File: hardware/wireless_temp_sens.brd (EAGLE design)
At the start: 100 x 80 mm, 32 parts, among them Q1 BC550C, Q2 32.768kHz, Q3 1MHz

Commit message: update board schema
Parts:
- removed C6, C7: 30pF, rcl:C025-024X044
- removed Q3: 1MHz, crystal:HC49/S
- moved C4 96.5 mm to (10.8, 22.4), turned to 90 degrees
- moved SUPPLY 86.7 mm to (15.7, 72.1), turned to 270 degrees
- moved UC1 65.5 mm to (75.2, 20.5), turned to 180 degrees
- moved R10 54.9 mm to (78.3, 38.8), turned to 270 degrees
- moved R9 52.3 mm to (78.3, 51.9), turned to 270 degrees
- moved C8 52.1 mm to (22.4, 23.9), turned to 180 degrees
- moved UC2 51.5 mm to (34.1, 13.5), turned to 0 degrees
- moved C1 51.0 mm to (57.2, 6.37), turned to 90 degrees
- moved C9 49.5 mm to (22.4, 15.8), turned to 180 degrees
- moved U$6 48.7 mm to (72.4, 49.6)
- moved R8 48.6 mm to (63.8, 48.6)
- moved C5 42.5 mm to (59.2, 48.4)
- moved R2 42.2 mm to (36.5, 5.43)
- moved R3 42.1 mm to (36.2, 9.13)
- moved UC3 41.5 mm to (44.1, 69.0), turned to 0 degrees
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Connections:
- net GND: no longer C6.2, C7.2
- net OSC1: no longer C6.1, Q3.2
- net OSC2: no longer C7.1, Q3.1
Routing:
- net BATTSENS: track 19.2 -> 60.3 mm, vias 2 -> 4
- net GND: track 335.9 -> 303.7 mm, vias 6 -> 0
- net UART_RX: track 81.5 -> 57.6 mm, vias 0 -> 2
- net VCC: track 185.6 -> 207.1 mm, vias 6 -> 4
- net N$4: track 54.4 -> 33.1 mm
- net N$7: track 4.32 -> 19.9 mm
- net LED_GREEN: track 4.06 -> 18.1 mm
- net SDA: track 34.2 -> 47.1 mm, vias 2 -> 4
- net SCL: track 53.2 -> 40.7 mm, vias 0 -> 2
- net N$1: track 33.0 -> 21.8 mm, vias 0 -> 2
- net UART_TX: track 83.0 -> 72.0 mm, vias 0 -> 2
- net PGC: track 3.81 -> 13.2 mm, vias 0 -> 2
- net N$6: track 6.10 -> 15.1 mm
- net PGD: track 4.17 -> 13.1 mm, vias 0 -> 2
- net PGM: track 3.81 -> 12.5 mm, vias 0 -> 2
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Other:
- board size 100 x 80 mm -> 90 x 83 mm

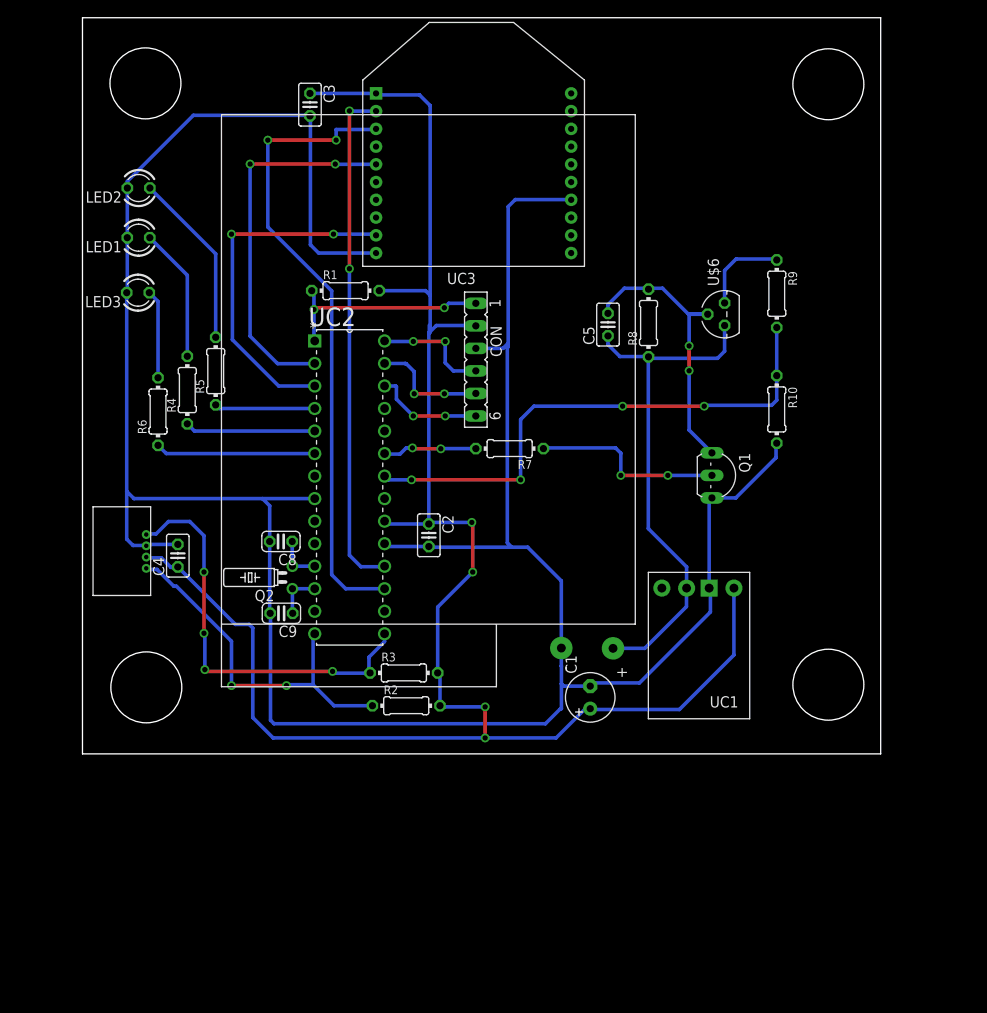
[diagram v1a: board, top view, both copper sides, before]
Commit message: update schematic with G300 box
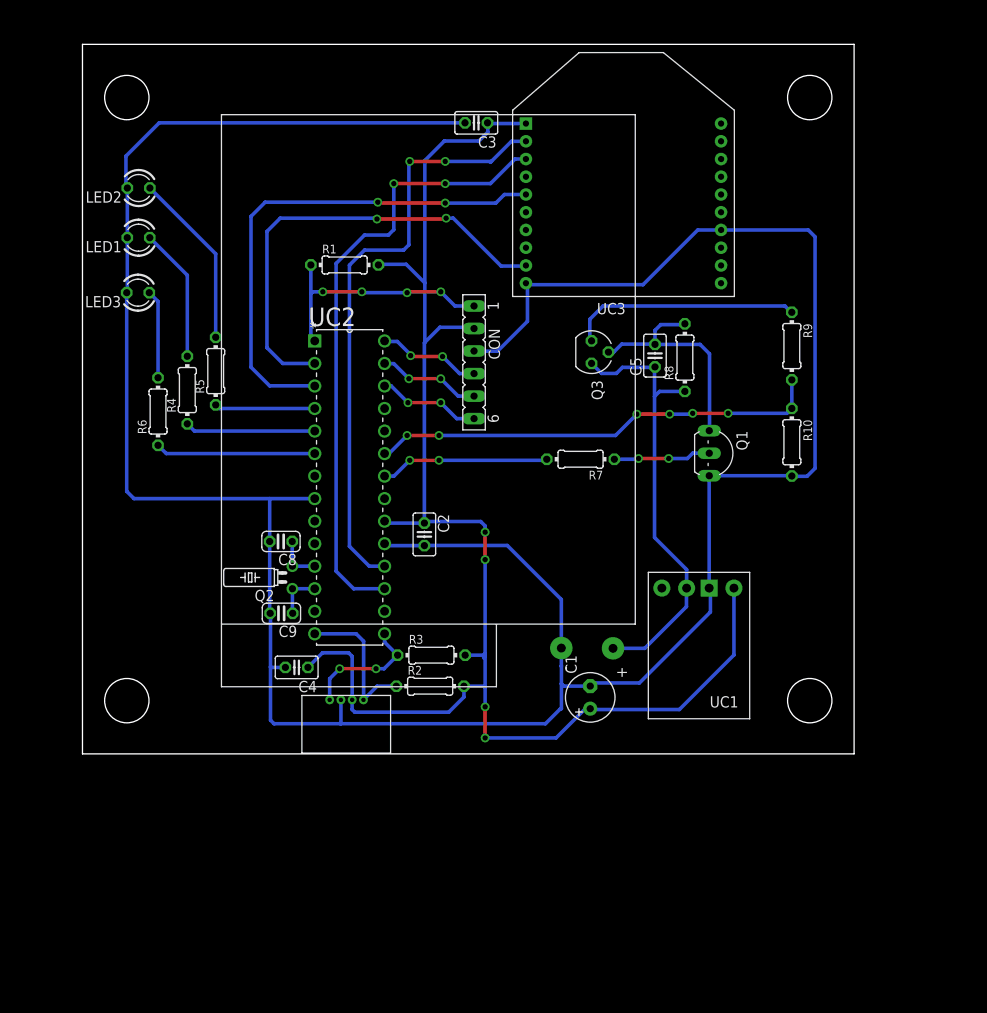
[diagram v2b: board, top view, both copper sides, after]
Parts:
- removed U$6: BS250P, ma_libs:TO92
- added Q3: BS250, transistor-small-signal:SOT54E
- moved UC4 27.3 mm to (24.7, 6.59), turned to 0 degrees
- moved C3 18.9 mm to (44.4, 71.2), turned to 180 degrees
- moved C4 18.4 mm to (24.1, 9.75), turned to 180 degrees
- moved UC3 17.2 mm to (61.0, 65.6)
- moved R7 8.09 mm to (56.2, 33.2)
- moved C5 6.35 mm to (64.5, 44.9)
- moved R9 6.14 mm to (80.0, 46.0)
- moved R8 5.66 mm to (67.9, 44.7)
- moved R10 4.07 mm to (80.0, 35.1)
- moved R3 3.69 mm to (39.3, 11.1)
- moved R2 3.48 mm to (39.2, 7.63)
- moved R1 2.90 mm to (29.6, 55.1)
- moved Q1 2.52 mm to (71.9, 33.9)
- moved C2 0.51 mm to (38.5, 24.8)
- moved CON 0.36 mm to (44.1, 44.1)
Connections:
- removed net N$5: R9.1, U$6.1
- new net N$3: Q3.D, R9.1
- net BATTSENS: now also UC2.23; no longer UC2.22
- net BATTSEN_EN: now also UC2.22; no longer UC2.23
- net N$4: now also Q3.G; no longer U$6.2
- net V_BATT: now also Q3.S; no longer U$6.3
- net XBEE_RESET: now also UC2.3; no longer UC2.2
- net XBEE_SLEEP_RQ: now also UC2.2; no longer UC2.3
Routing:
- net VCC: track 207.1 -> 174.0 mm
- net SDA: track 47.1 -> 14.2 mm, vias 4 -> 2
- net N$3: track 0.00 -> 26.2 mm
- net SCL: track 40.7 -> 16.8 mm, vias 2 -> 0
- net XBEE_RESET: track 42.2 -> 57.2 mm
- net GND: track 303.7 -> 318.5 mm
- net XBEE_SLEEP_RQ: track 39.7 -> 51.4 mm
- net N$1: track 21.8 -> 11.0 mm
- net UART_RX: track 57.6 -> 68.0 mm
- net N$5: track 10.1 -> 0.00 mm
- net BATTSENS: track 60.3 -> 51.2 mm, vias 4 -> 6
- net BATTSEN_EN: track 10.7 -> 19.1 mm
- net V_BATT: track 58.2 -> 50.3 mm
- net N$4: track 33.1 -> 26.2 mm, vias 2 -> 0
- net N$2: track 24.3 -> 28.0 mm, vias 2 -> 4
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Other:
- board size 90 x 83 mm -> 87 x 80 mm

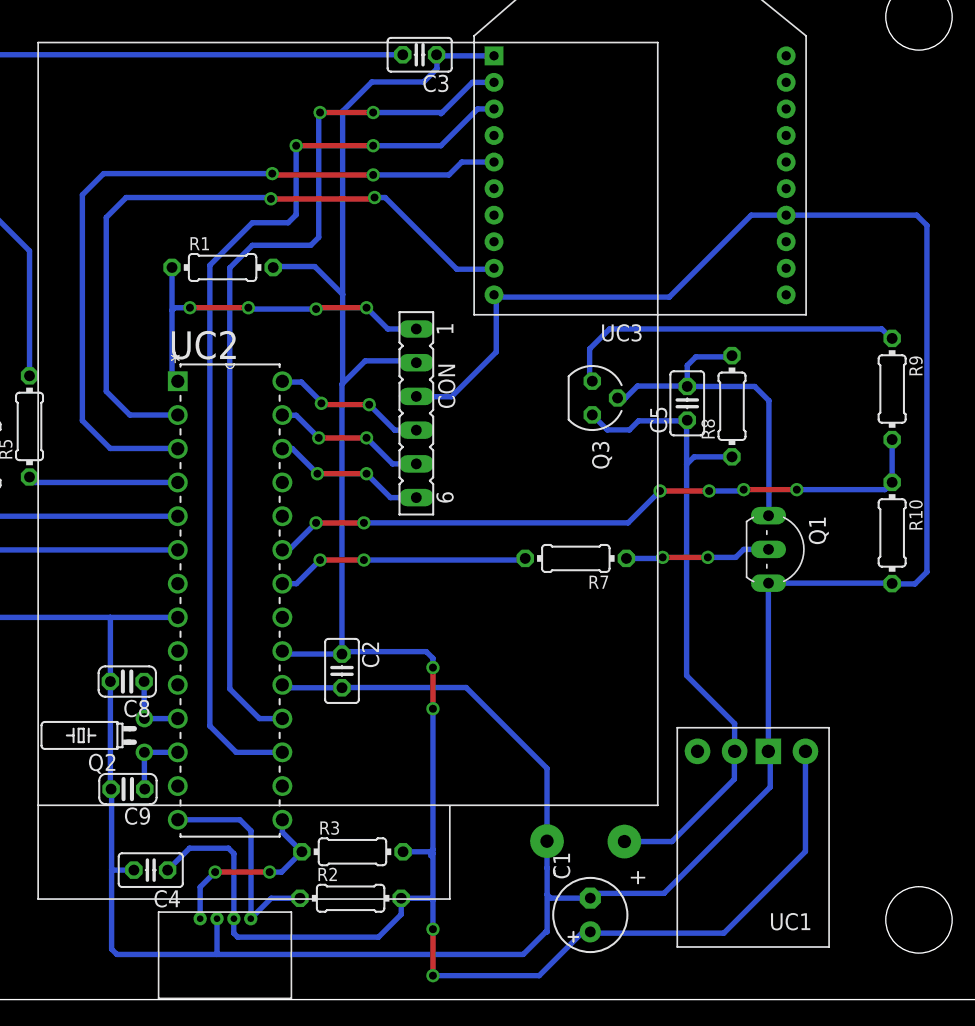
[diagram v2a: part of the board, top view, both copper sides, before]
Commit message: add 2.54mm connector for I2C
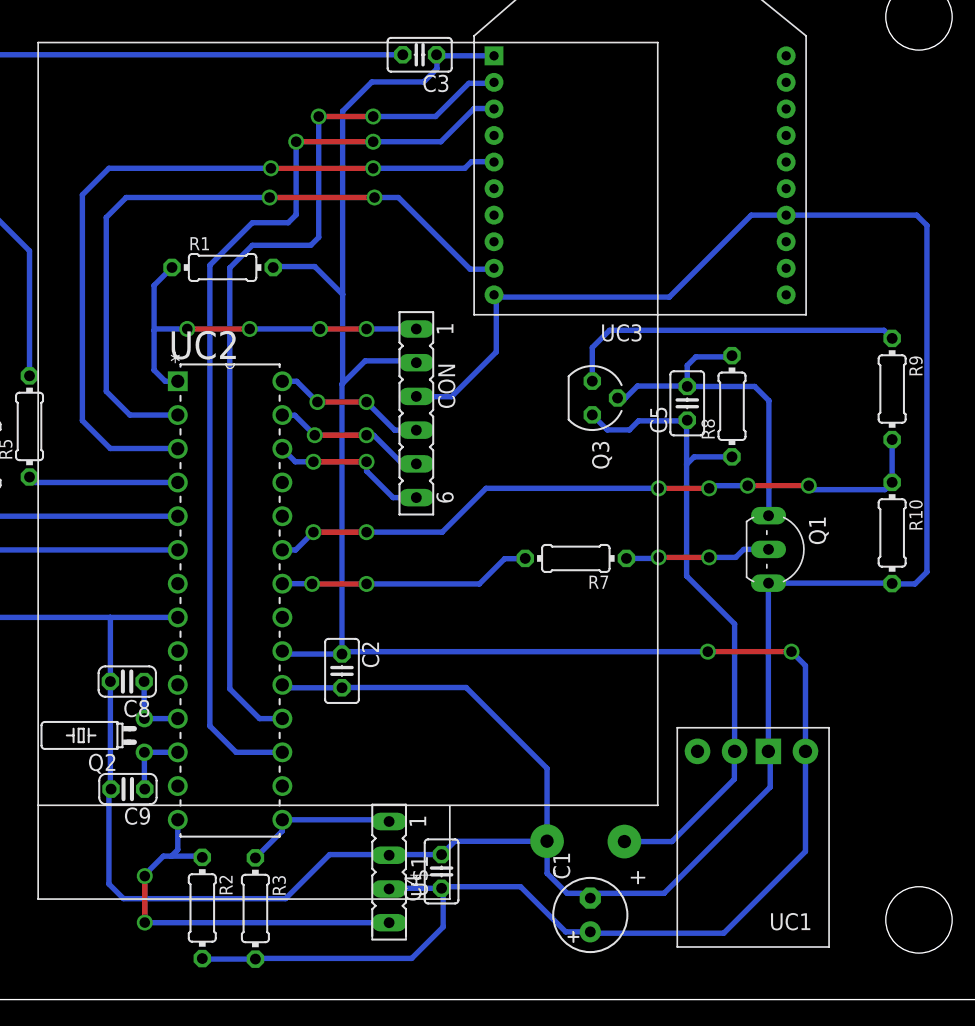
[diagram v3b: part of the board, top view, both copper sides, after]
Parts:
- removed UC4: HYT221, ma_libs:HYT221
- added U$1: HYT221HYT221-CON, ma_libs:HYT221-CON
- moved C4 21.9 mm to (46.0, 9.65), turned to 90 degrees
- moved R2 11.2 mm to (28.0, 6.90), turned to 270 degrees
- moved R3 8.47 mm to (32.0, 6.86), turned to 270 degrees
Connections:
- net GND: now also U$1.2; no longer UC4.GND
- net SCL: now also U$1.4; no longer UC4.SCL
- net SDA: now also U$1.1; no longer UC4.SDA
- net VCC: now also U$1.3; no longer UC4.VDD
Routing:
- net SCL: track 16.8 -> 29.9 mm, vias 0 -> 2
- net GND: track 318.5 -> 307.9 mm
- net VCC: track 174.0 -> 178.9 mm, vias 4 -> 2
- net SDA: track 14.2 -> 11.8 mm, vias 2 -> 0
- net N$2: track 28.0 -> 30.2 mm

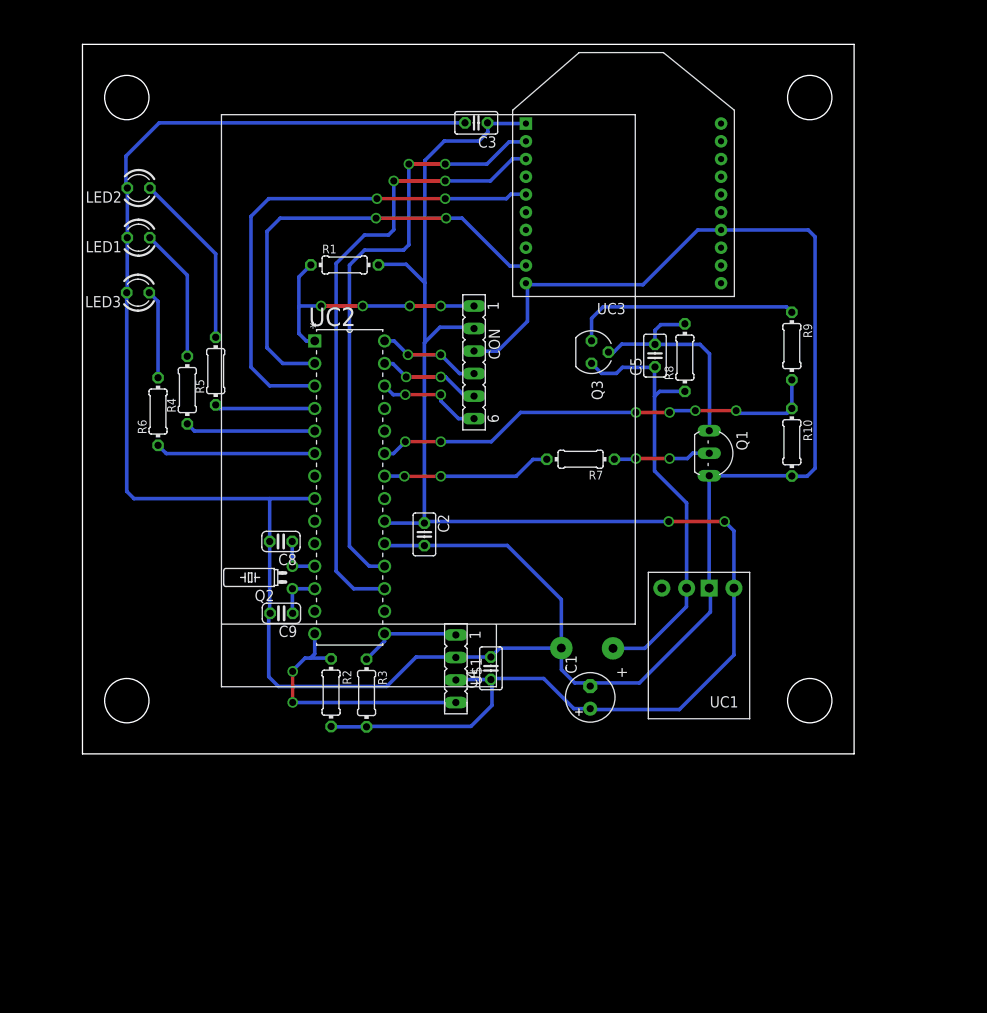
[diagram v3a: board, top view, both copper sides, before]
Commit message: update schematcks (width, drill and voltage fct emplacement
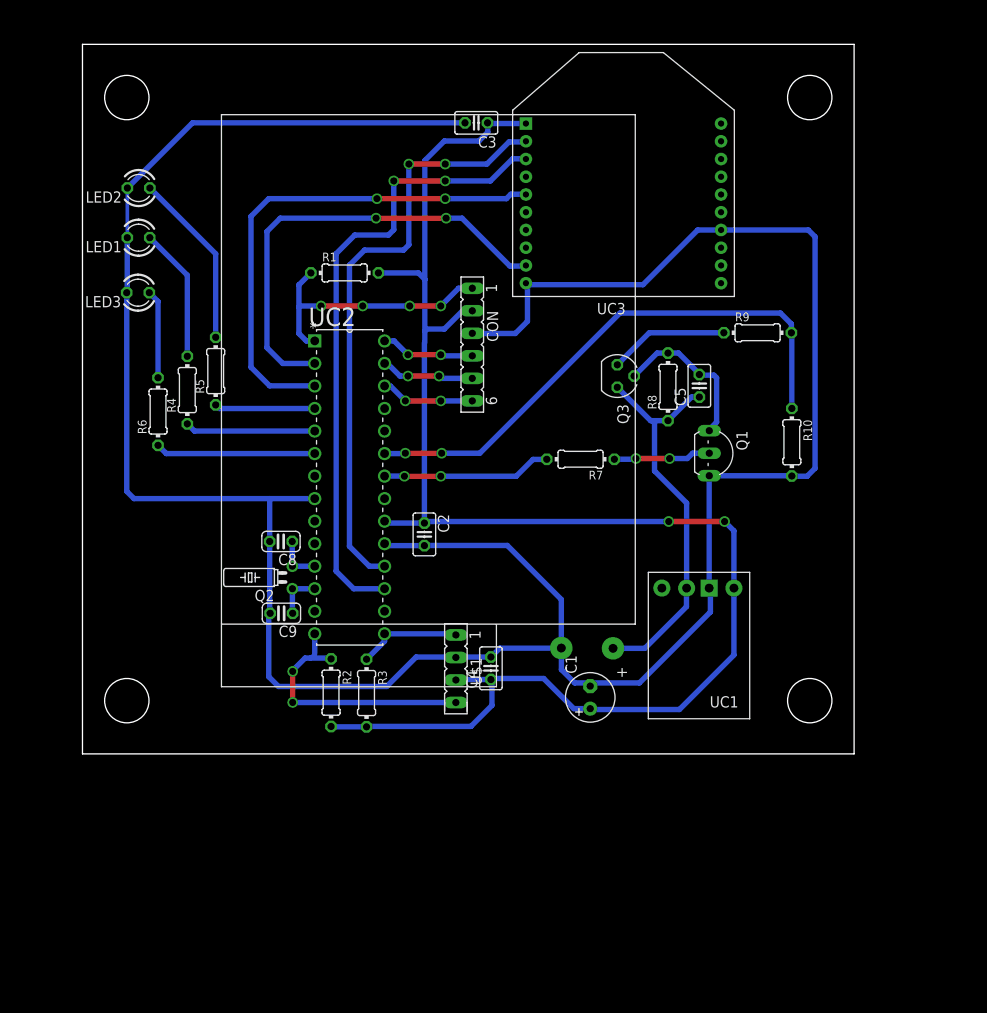
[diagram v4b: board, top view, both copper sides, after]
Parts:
- moved C5 6.05 mm to (69.5, 41.5)
- moved R9 4.14 mm to (76.1, 47.5), turned to 0 degrees
- moved Q3 3.96 mm to (60.3, 42.6)
- moved R8 3.81 mm to (66.0, 41.4)
- moved CON 2.01 mm to (44.0, 46.1)
- moved R1 0.90 mm to (29.6, 54.2)
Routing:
- net N$3: track 25.9 -> 13.5 mm
- net BATTSENS: track 51.5 -> 62.5 mm, vias 6 -> 2
- net N$4: track 26.2 -> 17.9 mm
- net V_BATT: track 50.3 -> 44.7 mm
- net GND: track 307.9 -> 304.9 mm
- net PGM: track 12.0 -> 10.7 mm
- net PGD: track 11.6 -> 10.7 mm
- net PGC: track 11.6 -> 10.8 mm
- net UART_TX: track 70.5 -> 71.1 mm
- net VCC: track 178.9 -> 178.3 mm

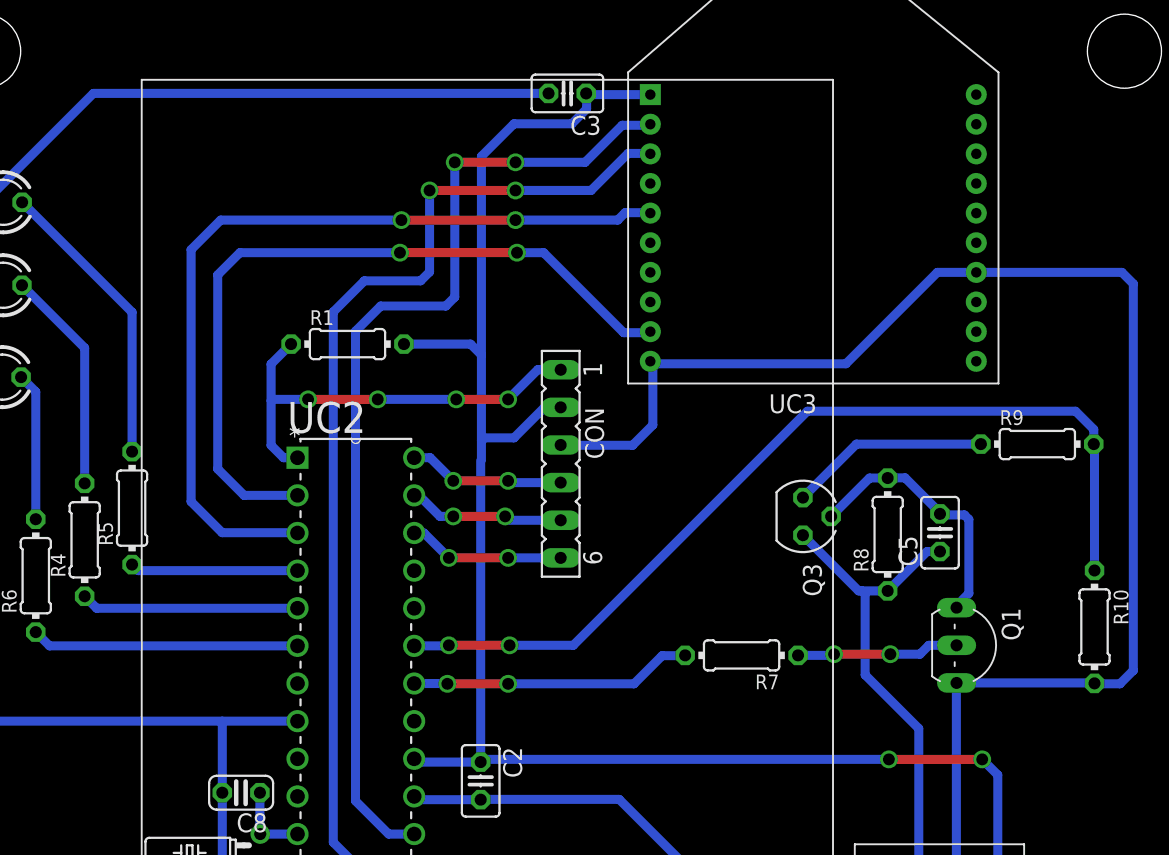
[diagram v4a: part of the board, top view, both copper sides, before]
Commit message: update resitor value or A/D conversion and update brd to remove some vias
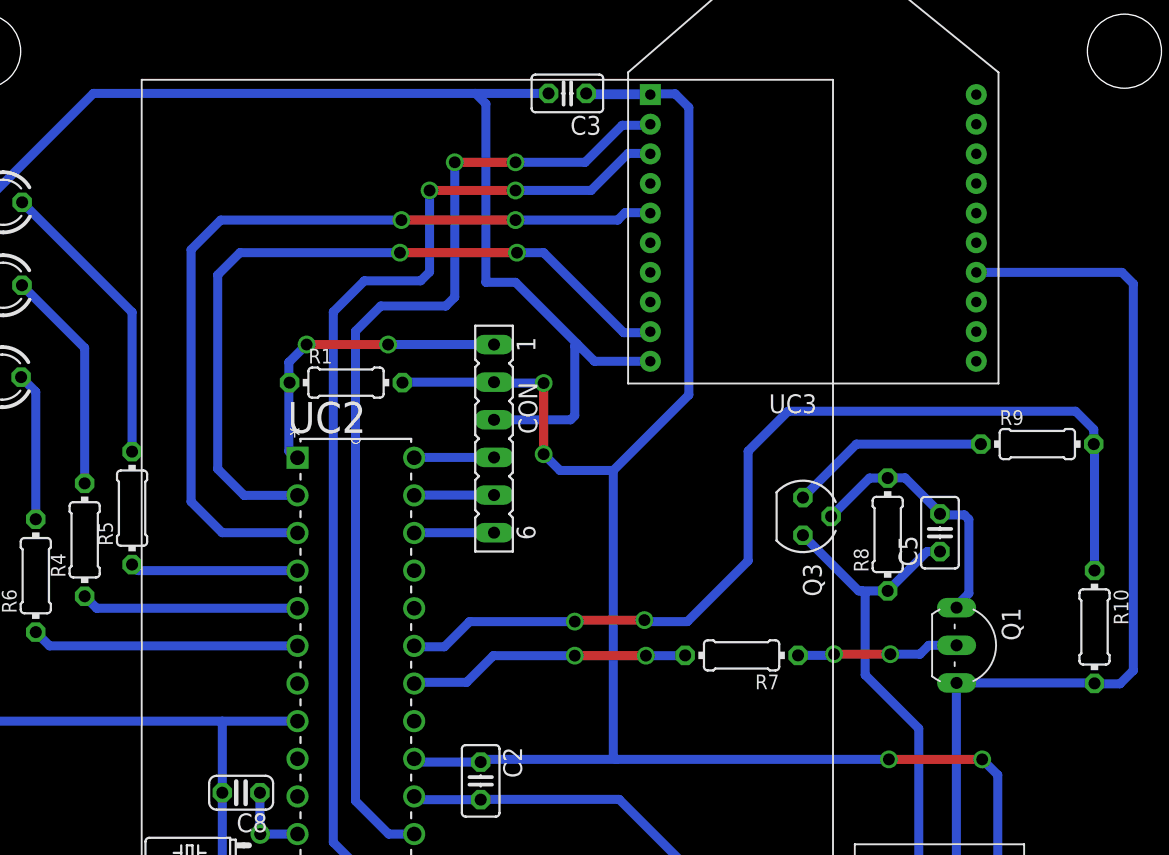
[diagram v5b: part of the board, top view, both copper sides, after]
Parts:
- R10: value 4.7k -> 2.2k
- R7: value 2k -> 10k
- R9: value 10k -> 4.7k
- moved CON 4.81 mm to (39.5, 47.9)
- moved R1 2.60 mm to (29.5, 51.6)
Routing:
- net VCC: track 178.3 -> 189.1 mm, vias 2 -> 4
- net N$2: track 29.9 -> 21.2 mm, vias 4 -> 2
- net PGC: track 10.8 -> 5.40 mm, vias 2 -> 0
- net PGM: track 10.7 -> 5.40 mm, vias 2 -> 0
- net PGD: track 10.7 -> 5.40 mm, vias 2 -> 0
- net BATTSENS: track 62.5 -> 66.9 mm
- net GND: track 304.9 -> 306.4 mm
